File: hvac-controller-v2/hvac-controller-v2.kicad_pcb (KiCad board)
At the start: 2 copper layers, 50 x 36 mm, 48 parts, among them J1 VAC IN, J2 Conn_01x06, J3 UART, U1 LY68L6400SLIT, U2 ESP32-PICO-D4, U4 TPS5430DDA, U5 TPS5430DDA, U6 LM324DT

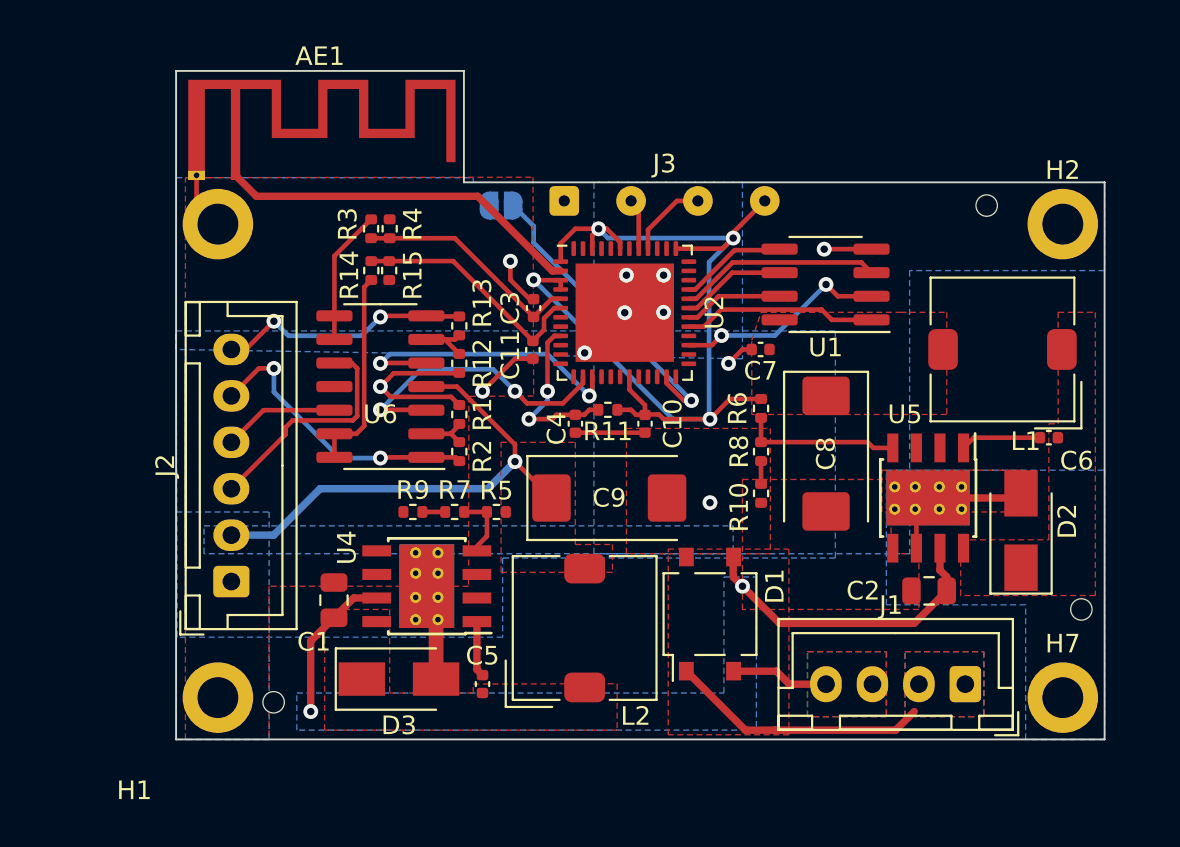
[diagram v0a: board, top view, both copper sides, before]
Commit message: Laid out board, sans boot jumper
Trying to figure out if I can hook this up to serial somehow.
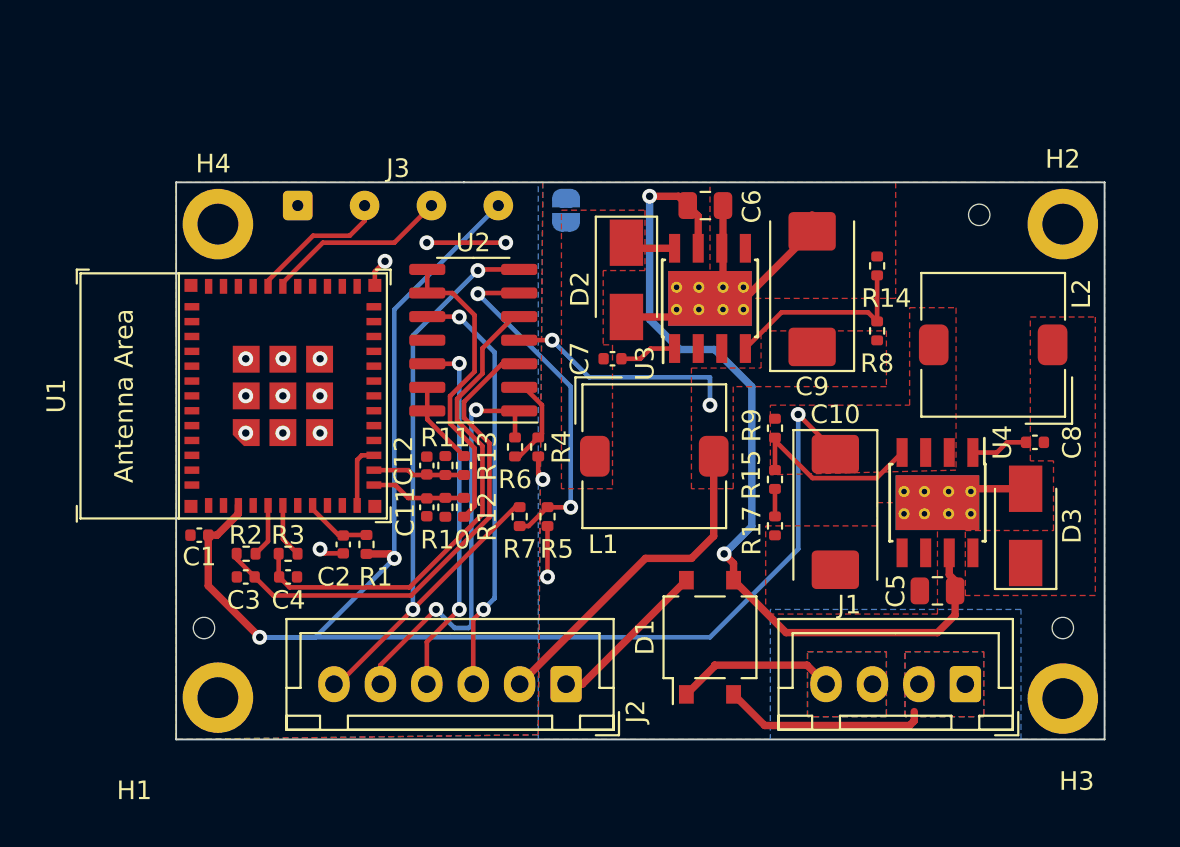
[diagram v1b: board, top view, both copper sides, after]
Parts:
- removed AE1: Antenna_Shield, kelvie:Texas_SWRA117D_2.4GHz_Right
- removed U5: TPS5430DDA, Package_SO:TI_SO-PowerPAD-8_ThermalVias
- removed U6: LM324DT, Package_SO:SOIC-14_3.9x8.7mm_P1.27mm
- added C12: 0.1uF, Capacitor_SMD:C_0402_1005Metric, F.Cu at (96.5, 101.8)
- added R17: 270, Resistor_SMD:R_0402_1005Metric, F.Cu at (115.2, 105.0)
- added U3: TPS5430DDA, Package_SO:TI_SO-PowerPAD-8_ThermalVias, F.Cu at (111.8, 92.8)
- C1: value 10uF/50V -> 0.01uF; footprint Capacitor_SMD:C_0805_2012Metric -> Capacitor_SMD:C_0402_1005Metric
- C10: value 0.01uF -> 470uF/6.3V; footprint Capacitor_SMD:C_0402_1005Metric -> Capacitor_Tantalum_SMD:CP_EIA-7343-31_Kemet-D
- C2: value 10uF/50V -> 1uF/5V; footprint Capacitor_SMD:C_0805_2012Metric -> Capacitor_SMD:C_0402_1005Metric
- C3: value 0.1uF -> 1uF/5V
- C5, C6: value 0.01uF -> 10uF/50V; footprint Capacitor_SMD:C_0402_1005Metric -> Capacitor_SMD:C_0805_2012Metric
- C7: value 0.1uF -> 0.01uF
- C8: value 470uF/6.3V -> 0.01uF; footprint Capacitor_Tantalum_SMD:CP_EIA-7343-31_Kemet-D -> Capacitor_SMD:C_0402_1005Metric
- C9: value 470uF/6.3V -> 100uF/16V
- H3, H4: value ToolingHole -> Hole; footprint kelvie:ToolingHole_1.152mm -> MountingHole:MountingHole_2.2mm_M2_DIN965_Pad
- H6, H7: value Hole -> ToolingHole; footprint MountingHole:MountingHole_2.2mm_M2_DIN965_Pad -> kelvie:ToolingHole_1.152mm
- R1: value 33k -> 10k
- R10: value 270 -> 18k
- R11: value 10k -> 18k
- R12: value 33k -> 2k
- R13: value 68k -> 2k
- R14, R3: value 18k -> 1.1k
- R15: value 2k -> 5.6k
- R2: value 68k -> 1.1k
- R4: value 2k -> 33k
- R5: value 10k -> 33k
- R6: value 10k -> 68k
- R7: value 1.1k -> 68k
- R8: value 5.6k -> 10k
- R9: value 33 -> 10k
- U1: value LY68L6400SLIT -> ESP32-C3-MINI-1; footprint Package_SO:SOIC-8_3.9x4.9mm_P1.27mm -> Espressif:ESP32-C3-MINI-1
- U2: value ESP32-PICO-D4 -> LM324DT; footprint Package_DFN_QFN:QFN-48-1EP_7x7mm_P0.5mm_EP5.3x5.3mm -> Package_SO:SOIC-14_3.9x8.7mm_P1.27mm
- moved H5 47.3 mm to (84.5, 110.5)
- moved H3 42.5 mm to (130.8, 114.3)
- moved H4 41.4 mm to (85.2, 88.8)
- moved H6 41.0 mm to (126.2, 88.2)
- moved D3 34.7 mm to (128.8, 105.0), turned to 90 degrees
- moved C2 31.6 mm to (92.0, 106.0), turned to -90 degrees
- moved U1 29.8 mm to (88.8, 98.0), turned to 90 degrees
- moved U4 27.9 mm to (124.0, 103.8), turned to -90 degrees
- moved R14 27.2 mm to (120.8, 91.0), turned to -90 degrees
- moved L2 26.8 mm to (127.0, 95.2), turned to 180 degrees
- moved D2 25.2 mm to (107.2, 91.8), turned to -90 degrees
- moved C5 25.0 mm to (124.0, 108.5), turned to 180 degrees
- moved R15 23.6 mm to (115.2, 102.5), turned to 90 degrees
- moved C6 22.3 mm to (111.5, 87.8)
- moved C3 21.2 mm to (86.8, 107.8), turned to 180 degrees
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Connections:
- C1 pad 1: /D1_OUT -> +3V3
- C10 pad 1: /VCC33 -> +3V3
- C11 pad 2: /ADC2 -> /ADC1
- C2 pad 1: /D1_OUT -> /CHIP_PU
- C3 pad 1: GND -> Net-(C3-Pad1)
- C3 pad 2: /ADC1 -> GND
- C4 pad 1: /CHIP_PU -> Net-(C4-Pad1)
- C5 pad 1: Net-(C5-Pad1) -> /D1_OUT
- C5 pad 2: /PH12 -> GND
- C6 pad 1: Net-(C6-Pad1) -> /D1_OUT
- C6 pad 2: /PH33 -> GND
- C7 pad 1: /VCC33 -> Net-(C7-Pad1)
- C7 pad 2: GND -> /PH12
- C8 pad 1: /VCC33 -> Net-(C8-Pad1)
- C8 pad 2: GND -> /PH33
- C9 pad 1: /VCC12 -> +12V
- D1 pad 1: /24VAC- -> -24VA
- D1 pad 2: /24VAC+ -> +24VA
- D2 pad 1: /PH33 -> /PH12
- D3 pad 1: /PH12 -> /PH33
- J1 pad 1: /24VAC- -> +24VA
- J1 pad 2: /24VAC- -> +24VA
- J1 pad 3: /24VAC+ -> -24VA
- J1 pad 4: /24VAC+ -> -24VA
- J2 pad 2: /VCC12 -> +12V
- J3 pad 4: /VCC33 -> +3V3
- L1 pad 1: /PH33 -> /PH12
- L1 pad 2: /VCC33 -> +12V
- L2 pad 1: /PH12 -> /PH33
- L2 pad 2: /VCC12 -> +3V3
- R1 pad 1: Net-(R1-Pad1) -> +3V3
- R1 pad 2: GND -> /CHIP_PU
- R10 pad 1: GND -> Net-(R10-Pad1)
- R10 pad 2: Net-(R8-Pad1) -> /ADC1
- R11 pad 1: /VCC33 -> Net-(R11-Pad1)
- R11 pad 2: /CHIP_PU -> /ADC2
- R12 pad 1: Net-(R12-Pad1) -> /ADC1
- R13 pad 1: Net-(R12-Pad1) -> /ADC2
- R13 pad 2: /CTRL2_OUT -> GND
- R14 pad 1: Net-(R14-Pad1) -> GND
- R14 pad 2: /ADC2 -> Net-(R14-Pad2)
- R15 pad 1: /ADC2 -> Net-(R15-Pad1)
- R15 pad 2: GND -> Net-(R15-Pad2)
- R2 pad 1: Net-(R1-Pad1) -> Net-(C3-Pad1)
- R2 pad 2: /CTRL1_OUT -> /PWM1
- R3 pad 1: Net-(R3-Pad1) -> Net-(C4-Pad1)
- R3 pad 2: /ADC1 -> /PWM2
- R4 pad 1: /ADC1 -> Net-(R4-Pad1)
- R5 pad 1: /VCC12 -> Net-(R5-Pad1)
- R5 pad 2: Net-(R7-Pad2) -> GND
- R6 pad 1: /VCC33 -> Net-(R4-Pad1)
- R6 pad 2: Net-(R8-Pad2) -> /CTRL1_OUT
- R7 pad 1: Net-(R7-Pad1) -> Net-(R5-Pad1)
- R7 pad 2: Net-(R7-Pad2) -> /CTRL2_OUT
- R8 pad 1: Net-(R8-Pad1) -> +12V
- R8 pad 2: Net-(R8-Pad2) -> Net-(R14-Pad2)
- R9 pad 1: GND -> +3V3
- R9 pad 2: Net-(R7-Pad1) -> Net-(R15-Pad2)
- U1 pad 1: /PSRAM_CS -> GND
- U1 pad 2: /SIO1 -> GND
- U1 pad 3: /SIO2 -> +3V3
- U1 pad 4: GND -> unconnected-(U1-Pad4)
- U1 pad 5: /SIO0 -> /PWM1
- U1 pad 6: /SCLK -> /PWM2
- U1 pad 7: /SIO3 -> unconnected-(U1-Pad7)
- U1 pad 8: /VCC33 -> /CHIP_PU
- U2 pad 1: /VCC33 -> /CTRL1_OUT
- U2 pad 10: unconnected-(U2-Pad10) -> /CTRL1_IN
- U2 pad 11: unconnected-(U2-Pad11) -> GND
- U2 pad 12: unconnected-(U2-Pad12) -> /CTRL2_IN
- U2 pad 13: unconnected-(U2-Pad13) -> Net-(R11-Pad1)
- U2 pad 14: /DAC1 -> Net-(R11-Pad1)
- U2 pad 2: Net-(AE1-Pad1) -> Net-(R4-Pad1)
- U2 pad 3: /VCC33 -> Net-(C3-Pad1)
- U2 pad 4: /VCC33 -> +12V
- U2 pad 5: /ADC1 -> Net-(C4-Pad1)
- U2 pad 6: /ADC2 -> Net-(R5-Pad1)
- U2 pad 7: unconnected-(U2-Pad7) -> /CTRL2_OUT
- U2 pad 8: unconnected-(U2-Pad8) -> Net-(R10-Pad1)
- U2 pad 9: /CHIP_PU -> Net-(R10-Pad1)
- U4 pad 1: Net-(C5-Pad1) -> Net-(C8-Pad1)
- U4 pad 4: Net-(R7-Pad2) -> Net-(R15-Pad2)
- U4 pad 8: /PH12 -> /PH33
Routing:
- net +3V3: track 0.00 -> 82.3 mm, vias 0 -> 3
- net /VCC33: track 55.5 -> 0.00 mm, vias 4 -> 0
- net +12V: track 0.00 -> 30.7 mm, vias 0 -> 2
- net Net-(C3-Pad1): track 0.00 -> 27.1 mm
- net Net-(C4-Pad1): track 0.00 -> 26.8 mm
- net /VCC12: track 26.7 -> 0.00 mm, vias 1 -> 0
- net /CTRL2_OUT: track 13.7 -> 35.7 mm
- net /D1_OUT: track 25.1 -> 46.6 mm
- net Net-(AE1-Pad1): track 19.6 -> 0.00 mm
- net Net-(R5-Pad1): track 0.00 -> 19.0 mm, vias 0 -> 2
- net /BOOT: track 16.5 -> 0.00 mm, vias 1 -> 0
- net Net-(R10-Pad1): track 0.00 -> 16.5 mm
- net /DAC2: track 16.0 -> 0.00 mm, vias 2 -> 0
- net /DAC1: track 15.9 -> 0.00 mm, vias 2 -> 0
- net /24VAC-: track 14.0 -> 0.00 mm
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- added copper zone on F.Cu, net +12V
- added copper zone on B.Cu, net +24VA
- added copper zone on F.Cu, net +24VA
- added copper zone on F.Cu, net +3V3
- added copper zone on B.Cu, net -24VA
- added copper zone on F.Cu, net -24VA
- removed copper zone on B.Cu, net /24VAC+
- removed copper zone on F.Cu, net /24VAC+
- removed copper zone on B.Cu, net /24VAC-
- removed copper zone on F.Cu, net /24VAC-
- removed copper zone on B.Cu, net /D1_OUT
- removed copper zone on F.Cu, net /VCC12
- removed copper zone on F.Cu, net /VCC33
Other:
- board size 50 x 36 mm -> 50 x 30 mm

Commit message: Silkscreen clean up.
I think I want to move the antenna to the top edge though
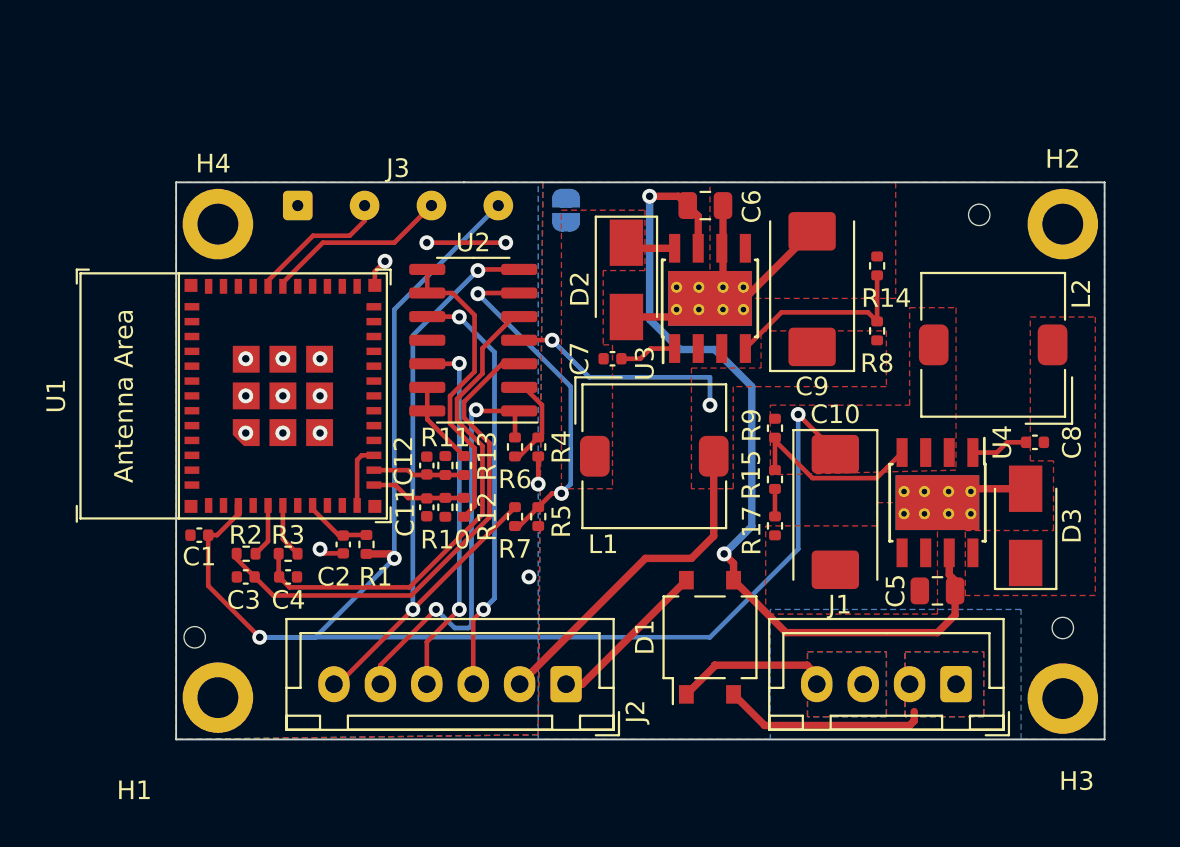
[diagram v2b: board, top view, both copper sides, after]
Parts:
- moved H5 0.71 mm to (84.0, 111.0)
- moved J1 0.50 mm to (125.0, 113.5)
- moved R5 0.50 mm to (102.5, 104.5)
- moved R7 0.25 mm to (101.2, 104.5)
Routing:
- net GND: track 45.7 -> 42.2 mm
- net Net-(R5-Pad1): track 19.0 -> 18.3 mm
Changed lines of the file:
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@@
   )
   (footprint "Connector_JST:JST_XH_B4B-XH-A_1x04_P2.50mm_Vertical" (layer "F.Cu")
-    (at 125.5 113.525 180)
+    (at 125 113.525 180)
     (descr "JST XH series connector, B4B-XH-A (http://www.jst-mfg.com/product/pdf/eng/eXH.pdf), generated with kicad-footprint-generator")
     (tags "connector JST XH vertical")
@@
   )
   (footprint "Resistor_SMD:R_0402_1005Metric" (layer "F.Cu")
-    (at 103 104.5 -90)
+    (at 102.5 104.5 -90)
     (descr "Resistor SMD 0402 (1005 Metric), square (rectangular) end terminal, IPC_7351 nominal, (Body size source: IPC-SM-782 page 72, https://www.pcb-3d.com/wordpress/wp-content/uploads/ipc-sm-782a_amendment_1_and_2.pdf), generated with kicad-footprint-generator")
     (tags "resistor")
@@
     (property "Sheetname" "")
     (attr smd)
-    (fp_text reference "R5" (at 1.75 -0.5 180) (layer "F.SilkS")
+    (fp_text reference "R5" (at 0.25 -1.25 -90) (layer "F.SilkS")
       (effects (font (size 1 1) (thickness 0.15)))
     )
@@
   )
   (footprint "Resistor_SMD:R_0402_1005Metric" (layer "F.Cu")
-    (at 101.5 104.5 90)
+    (at 101.25 104.5 90)
     (descr "Resistor SMD 0402 (1005 Metric), square (rectangular) end terminal, IPC_7351 nominal, (Body size source: IPC-SM-782 page 72, https://www.pcb-3d.com/wordpress/wp-content/uploads/ipc-sm-782a_amendment_1_and_2.pdf), generated with kicad-footprint-generator")
     (tags "resistor")
@@
   )
   (footprint "kelvie:ToolingHole_1.152mm" (layer "F.Cu")
-    (at 84.5 110.5)
+    (at 84 111)
     (descr "Mounting Hole 2.1mm, no annular")
     (tags "mounting hole 2.1mm no annular")
@@
     (style (thickness 0.15) (arrow_length 1.27) (text_position_mode 0) (extension_height 0.58642) (extension_offset 0.5) keep_text_aligned)
   )
-  (segment (start 84.73 105.5) (end 85.203022 105.5) (width 0.4) (layer "F.Cu") (net 1))
+  (segment (start 84.73 105.5) (end 85.203022 105.5) (width 0.25) (layer "F.Cu") (net 1))
   (segment (start 93.25 106.51) (end 94.51 106.51) (width 0.4) (layer "F.Cu") (net 1))
-  (segment (start 84.73 105.5) (end 84.73 108.23) (width 0.4) (layer "F.Cu") (net 1))
+  (segment (start 84.73 105.5) (end 84.73 108.23) (width 0.25) (layer "F.Cu") (net 1))
   (segment (start 118.5 101) (end 116.5 99) (width 0.25) (layer "F.Cu") (net 1))
-  (segment (start 85.203022 105.5) (end 86.35 104.353022) (width 0.4) (layer "F.Cu") (net 1))
+  (segment (start 85.203022 105.5) (end 86.35 104.353022) (width 0.25) (layer "F.Cu") (net 1))
   (segment (start 118.5 101.1375) (end 118.5 101) (width 0.25) (layer "F.Cu") (net 1))
-  (segment (start 84.73 108.23) (end 87.5 111) (width 0.4) (layer "F.Cu") (net 1))
+  (segment (start 84.73 108.23) (end 87.5 111) (width 0.25) (layer "F.Cu") (net 1))
   (segment (start 94.51 106.51) (end 94.75 106.75) (width 0.4) (layer "F.Cu") (net 1))
   (segment (start 86.35 104.353022) (end 86.35 103.9) (width 0.4) (layer "F.Cu") (net 1))
@@
   (segment (start 111.75 97) (end 111.75 98.5) (width 0.25) (layer "B.Cu") (net 2))
   (segment (start 92.75 101.45) (end 93 101.2) (width 0.25) (layer "F.Cu") (net 3))
-  (segment (start 102.5 101.26) (end 102.5 102.25) (width 0.25) (layer "F.Cu") (net 3))
-  (segment (start 117.25 89.1375) (end 117.25 88.25) (width 0.4) (layer "F.Cu") (net 3))
+  (segment (start 102.5 101.26) (end 102.5 102.75) (width 0.25) (layer "F.Cu") (net 3))
   (segment (start 90.98 106.48) (end 90.75 106.25) (width 0.25) (layer "F.Cu") (net 3))
-  (segment (start 103 105.01) (end 103 107.75) (width 0.25) (layer "F.Cu") (net 3))
   (segment (start 117.25 89.1375) (end 113.6375 92.75) (width 0.4) (layer "F.Cu") (net 3))
   (segment (start 107.25 93.75) (end 110.75 93.75) (width 0.4) (layer "F.Cu") (net 3))
@@
   (segment (start 93.7 91.3) (end 94.25 90.75) (width 0.25) (layer "F.Cu") (net 3))
   (segment (start 104 113.525) (end 104.88 113.525) (width 0.4) (layer "F.Cu") (net 3))
-  (segment (start 102.5 102.25) (end 102.75 102.5) (width 0.25) (layer "F.Cu") (net 3))
   (segment (start 104.88 113.525) (end 110.48 107.925) (width 0.4) (layer "F.Cu") (net 3))
   (segment (start 124.75 103) (end 124 103.75) (width 0.4) (layer "F.Cu") (net 3))
@@
   (via (at 94.25 90.75) (size 0.8) (drill 0.4) (layers "F.Cu" "B.Cu") (net 3))
   (via (at 100.75 89.75) (size 0.8) (drill 0.4) (layers "F.Cu" "B.Cu") (free) (net 3))
-  (via (at 103 107.75) (size 0.8) (drill 0.4) (layers "F.Cu" "B.Cu") (net 3))
+  (via (at 102 107.75) (size 0.8) (drill 0.4) (layers "F.Cu" "B.Cu") (net 3))
   (via (at 88.75 96) (size 0.8) (drill 0.4) (layers "F.Cu" "B.Cu") (net 3))
   (via (at 90.75 106.25) (size 0.8) (drill 0.4) (layers "F.Cu" "B.Cu") (net 3))
@@
   (via (at 88.75 98) (size 0.8) (drill 0.4) (layers "F.Cu" "B.Cu") (net 3))
   (via (at 86.75 100) (size 0.8) (drill 0.4) (layers "F.Cu" "B.Cu") (net 3))
-  (via (at 102.75 102.5) (size 0.8) (drill 0.4) (layers "F.Cu" "B.Cu") (net 3))
+  (via (at 102.5 102.75) (size 0.8) (drill 0.4) (layers "F.Cu" "B.Cu") (net 3))
   (via (at 88.75 100) (size 0.8) (drill 0.4) (layers "F.Cu" "B.Cu") (net 3))
   (segment (start 127.2 101.05) (end 127.75 100.5) (width 0.25) (layer "F.Cu") (net 4))
@@
   (segment (start 101.48 101.26) (end 102.5 100.24) (width 0.25) (layer "F.Cu") (net 25))
   (segment (start 102.70152 100.03848) (end 102.70152 98.493685) (width 0.25) (layer "F.Cu") (net 25))
-  (segment (start 101.26 103.99) (end 101.5 103.99) (width 0.25) (layer "F.Cu") (net 26))
   (segment (start 99.31 91.19) (end 99.25 91.25) (width 0.25) (layer "F.Cu") (net 26))
   (segment (start 91.725 113.525) (end 95.75 109.5) (width 0.25) (layer "F.Cu") (net 26))
@@
   (segment (start 100.151501 108.9015) (end 99.553001 109.5) (width 0.25) (layer "B.Cu") (net 28))
   (segment (start 98.25 93.75) (end 100.151501 95.651501) (width 0.25) (layer "B.Cu") (net 28))
-  (segment (start 104.25 104) (end 103.01 104) (width 0.25) (layer "F.Cu") (net 29))
-  (segment (start 101.5 105.01) (end 101.98 105.01) (width 0.25) (layer "F.Cu") (net 29))
   (segment (start 99.29 92.46) (end 99.25 92.5) (width 0.25) (layer "F.Cu") (net 29))
+  (segment (start 101.5 105.01) (end 101.5 104.995) (width 0.25) (layer "F.Cu") (net 29))
+  (segment (start 103.245 103.25) (end 103.75 103.25) (width 0.25) (layer "F.Cu") (net 29))
   (segment (start 101.475 92.46) (end 99.29 92.46) (width 0.25) (layer "F.Cu") (net 29))
-  (segment (start 103.01 104) (end 103 103.99) (width 0.25) (layer "F.Cu") (net 29))
-  (segment (start 101.98 105.01) (end 103 103.99) (width 0.25) (layer "F.Cu") (net 29))
-  (via (at 104.25 104) (size 0.8) (drill 0.4) (layers "F.Cu" "B.Cu") (net 29))
+  (segment (start 101.5 104.995) (end 103.245 103.25) (width 0.25) (layer "F.Cu") (net 29))
+  (via (at 103.75 103.25) (size 0.8) (drill 0.4) (layers "F.Cu" "B.Cu") (net 29))
   (via (at 99.25 92.5) (size 0.8) (drill 0.4) (layers "F.Cu" "B.Cu") (net 29))
+  (segment (start 104.25 102.75) (end 103.75 103.25) (width 0.25) (layer "B.Cu") (net 29))
+  (segment (start 104.25 97.5) (end 104.25 102.75) (width 0.25) (layer "B.Cu") (net 29))
   (segment (start 99.25 92.5) (end 104.25 97.5) (width 0.25) (layer "B.Cu") (net 29))
-  (segment (start 104.25 97.5) (end 104.25 104) (width 0.25) (layer "B.Cu") (net 29))
   (segment (start 120.75 91.51) (end 120.75 93.99) (width 0.25) (layer "F.Cu") (net 30))
   (segment (start 120.75 93.99) (end 120.26 93.5) (width 0.25) (layer "F.Cu") (net 30))
